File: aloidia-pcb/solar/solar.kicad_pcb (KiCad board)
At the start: 2 copper layers, 132 x 13.8 mm, 6 parts, among them J1 SM04B-SRSS-TB(LF)(SN)

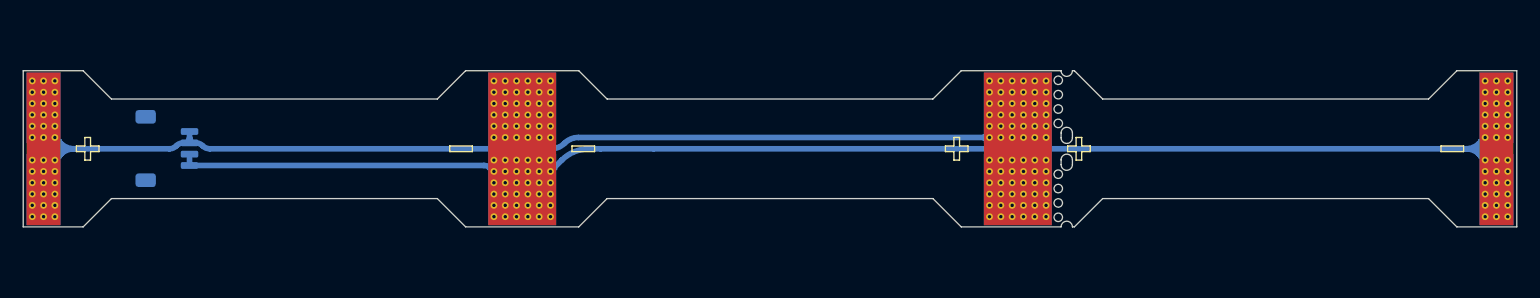
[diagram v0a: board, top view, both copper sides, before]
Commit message: Added cutouts to solar PCB for screw clearance
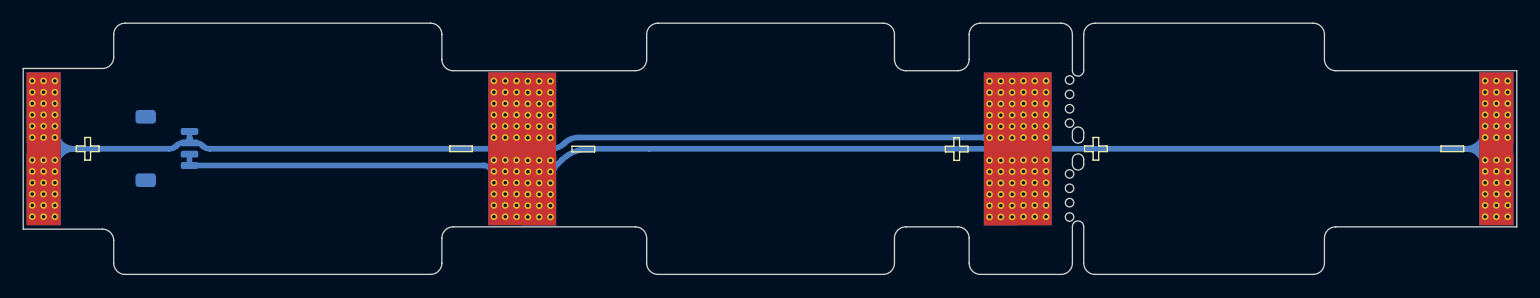
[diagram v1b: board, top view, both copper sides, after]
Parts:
- moved REF** 1.00 mm to (180.5, 89.1)
- moved REF** 1.00 mm to (180.5, 80.8)
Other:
- board size 132 x 13.8 mm -> 132 x 22.2 mm
